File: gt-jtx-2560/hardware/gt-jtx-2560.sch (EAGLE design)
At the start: 21 parts

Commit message: added new files
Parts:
- removed LCD1: LCD-G12864-BARE, SparkFun-Displays:LCD-G12864-BARE
- added J1: (no value), SparkFun-Connectors:CONN_20
- added R1: 2.2K, resistor:R-US_0204/5
- added R2: 1K, resistor:R-US_0204/5
- added ROT_1, ROT_2: rgSbVBCA, Rembrandt Electronics - JST XH Connectors v1-0:JST-XH-08-PIN-LONG-PAD
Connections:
- new net N$31: B1.15(RX3), ROT_1-3.S
- new net N$47: B1.14(TX3), ROT_2-3.S
- new net N$48: B1.2, ROT_1-8.S
- new net N$49: B1.3, ROT_1-6.S
- new net N$50: B1.19(RX1), ROT_2-8.S
- new net N$51: B1.18(TX1), ROT_2-6.S
- new net N$52: J1.19, R1.1
- new net N$53: B1.30, J1.6
- new net N$54: B1.31, J1.16
- new net N$55: B1.32, J1.4
- new net N$56: B1.33, J1.17
- new net N$57: B1.34, J1.15
- new net N$58: J1.5, R2.1
- net N$1: now also J1.7; no longer LCD1.DB0
- net N$2: now also J1.8; no longer LCD1.DB1
- net N$3: now also J1.9; no longer LCD1.DB2
- net N$4: now also J1.10; no longer LCD1.DB3
- net N$43: now also J1.1, J1.20, R2.2, ROT_1-7.S, ROT_2-7.S
- net N$44: now also J1.2, R1.2, ROT_1-5.S, ROT_2-5.S
- net N$5: now also J1.11; no longer LCD1.DB4
- net N$6: now also J1.12; no longer LCD1.DB5
- net N$7: now also J1.13; no longer LCD1.DB6
- net N$8: now also J1.14; no longer LCD1.DB7
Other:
- moved on the sheet: NAVI-7

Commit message: added case design, changed the schematic for lcd
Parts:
- added ID1, ID2: JST-XH-03-PIN-LONG-PAD, Rembrandt Electronics - JST XH Connectors v1-0:JST-XH-03-PIN-LONG-PAD
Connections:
- removed net N$43: AIL-3.S, AIL_DR-3.S, B1.GND@0, B1.GND@1, B1.GND@2, B1.GND@3, B1.GND@4, ELE-3.S, ELE_DR-3.S, GEAR-3.S, H_B-3.S, J1.1, J1.20, NAVI-8.S, POT1-3.S, POT2-3.S, POT3-3.S, PPM-3.S, R2.2, ROT_1-7.S, ROT_2-7.S, RUD-3.S, RUD_DR-3.S, SD-6.S, THR-3.S, THR_X-3.S, TRIML-8.S, TRIMR-8.S, TRN-3.S
- removed net N$44: AIL-1.S, AIL_DR-1.S, B1.5V@0, B1.AREF, ELE-1.S, ELE_DR-1.S, GEAR-1.S, J1.2, NAVI-1.S, POT1-1.S, POT2-1.S, POT3-1.S, PPM-2.S, R1.2, ROT_1-5.S, ROT_2-5.S, RUD-1.S, RUD_DR-1.S, SD-5.S, THR-1.S, THR_X-1.S, TRIML-1.S, TRIMR-1.S, TRN-1.S
- new net GND: AIL-3.S, AIL_DR-3.S, B1.GND@0, B1.GND@1, B1.GND@2, B1.GND@3, B1.GND@4, ELE-3.S, ELE_DR-3.S, GEAR-3.S, H_B-3.S, ID1-3.S, ID2-3.S, J1.1, J1.20, NAVI-8.S, POT1-3.S, POT2-3.S, POT3-3.S, PPM-3.S, R2.2, ROT_1-7.S, ROT_2-7.S, RUD-3.S, RUD_DR-3.S, SD-6.S, THR-3.S, THR_X-3.S, TRIML-8.S, TRIMR-8.S, TRN-3.S
- new net N$59: B1.36, ID2-2.S
- new net N$60: B1.37, ID1-2.S
- new net VCC: AIL-1.S, AIL_DR-1.S, B1.5V@0, B1.AREF, ELE-1.S, ELE_DR-1.S, GEAR-1.S, ID1-1.S, ID2-1.S, J1.2, NAVI-1.S, POT1-1.S, POT2-1.S, POT3-1.S, PPM-2.S, R1.2, ROT_1-5.S, ROT_2-5.S, RUD-1.S, RUD_DR-1.S, SD-5.S, THR-1.S, THR_X-1.S, TRIML-1.S, TRIMR-1.S, TRN-1.S
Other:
- moved on the sheet: PPM-2, R1, ROT_1-1, ROT_1-2, ROT_1-4
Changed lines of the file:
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@@
 <?xml version="1.0" encoding="utf-8"?>
 <!DOCTYPE eagle SYSTEM "eagle.dtd">
-<eagle version="8.1.0">
+<eagle version="8.2.2">
 <drawing>
 <settings>
@@
 <part name="R1" library="resistor" deviceset="R-US_" device="0204/5" value="2.2K"/>
 <part name="R2" library="resistor" deviceset="R-US_" device="0204/5" value="1K"/>
+<part name="ID2" library="Rembrandt Electronics - JST XH Connectors v1-0" deviceset="JST-XH-03-PIN" device="-LONG-PAD" value=""/>
+<part name="ID1" library="Rembrandt Electronics - JST XH Connectors v1-0" deviceset="JST-XH-03-PIN" device="-LONG-PAD" value=""/>
 </parts>
 <sheets>
@@
 <instance part="H_B" gate="-3" x="116.84" y="15.24" rot="R90"/>
 <instance part="PPM" gate="-1" x="2.54" y="63.5" rot="R180"/>
-<instance part="PPM" gate="-2" x="132.08" y="160.02" rot="R270"/>
+<instance part="PPM" gate="-2" x="124.46" y="160.02" rot="R270"/>
 <instance part="PPM" gate="-3" x="119.38" y="15.24" rot="R90"/>
 <instance part="B1" gate="G$1" x="22.86" y="101.6"/>
@@
 <instance part="SD" gate="-7" x="-17.78" y="111.76" rot="R180"/>
 <instance part="SD" gate="-8" x="-17.78" y="109.22" rot="R180"/>
-<instance part="ROT_1" gate="-1" x="119.38" y="121.92"/>
-<instance part="ROT_1" gate="-2" x="119.38" y="119.38"/>
+<instance part="ROT_1" gate="-1" x="111.76" y="121.92"/>
+<instance part="ROT_1" gate="-2" x="111.76" y="119.38"/>
 <instance part="ROT_1" gate="-3" x="43.18" y="147.32"/>
-<instance part="ROT_1" gate="-4" x="119.38" y="114.3"/>
+<instance part="ROT_1" gate="-4" x="111.76" y="114.3"/>
 <instance part="ROT_1" gate="-5" x="93.98" y="160.02" rot="R270"/>
 <instance part="ROT_1" gate="-6" x="2.54" y="86.36" rot="R180"/>
@@
 <attribute name="NAME" x="81.28" y="93.472" size="1.778" layer="95" font="vector" rot="R180"/>
 </instance>
-<instance part="R1" gate="G$1" x="129.54" y="99.06"/>
+<instance part="R1" gate="G$1" x="116.84" y="99.06"/>
 <instance part="R2" gate="G$1" x="86.36" y="139.7" rot="R90"/>
+<instance part="ID2" gate="-1" x="139.7" y="160.02" rot="MR270"/>
+<instance part="ID2" gate="-2" x="43.18" y="93.98" rot="MR180"/>
+<instance part="ID2" gate="-3" x="139.7" y="15.24" rot="MR90"/>
+<instance part="ID1" gate="-1" x="137.16" y="160.02" rot="MR270"/>
+<instance part="ID1" gate="-2" x="43.18" y="91.44" rot="MR180"/>
+<instance part="ID1" gate="-3" x="142.24" y="15.24" rot="MR90"/>
 </instances>
 <busses>
@@
 </segment>
 </net>
-<net name="N$43" class="0">
+<net name="GND" class="0">
 <segment>
 <pinref part="B1" gate="G$1" pin="GND@0"/>
@@
 <junction x="116.84" y="12.7"/>
 <pinref part="PPM" gate="-3" pin="S"/>
-<wire x1="119.38" y1="12.7" x2="147.32" y2="12.7" width="0.1524" layer="91"/>
+<wire x1="119.38" y1="12.7" x2="139.7" y2="12.7" width="0.1524" layer="91"/>
 <junction x="119.38" y="12.7"/>
+<wire x1="139.7" y1="12.7" x2="142.24" y2="12.7" width="0.1524" layer="91"/>
+<wire x1="142.24" y1="12.7" x2="147.32" y2="12.7" width="0.1524" layer="91"/>
 <wire x1="5.08" y1="50.8" x2="5.08" y2="12.7" width="0.1524" layer="91"/>
 <junction x="5.08" y="50.8"/>
@@
 <pinref part="R2" gate="G$1" pin="2"/>
 <junction x="86.36" y="144.78"/>
-</segment>
-</net>
-<net name="N$44" class="0">
+<pinref part="ID1" gate="-3" pin="S"/>
+<junction x="142.24" y="12.7"/>
+<pinref part="ID2" gate="-3" pin="S"/>
+<junction x="139.7" y="12.7"/>
+</segment>
+</net>
+<net name="VCC" class="0">
 <segment>
 <wire x1="0" y1="139.7" x2="0" y2="149.86" width="0.1524" layer="91"/>
@@
 <junction x="144.78" y="162.56"/>
 <pinref part="POT3" gate="-1" pin="S"/>
-<wire x1="142.24" y1="162.56" x2="137.16" y2="162.56" width="0.1524" layer="91"/>
+<wire x1="142.24" y1="162.56" x2="139.7" y2="162.56" width="0.1524" layer="91"/>
 <junction x="142.24" y="162.56"/>
 <pinref part="GEAR" gate="-1" pin="S"/>
-<wire x1="137.16" y1="162.56" x2="132.08" y2="162.56" width="0.1524" layer="91"/>
+<wire x1="139.7" y1="162.56" x2="137.16" y2="162.56" width="0.1524" layer="91"/>
+<wire x1="137.16" y1="162.56" x2="129.54" y2="162.56" width="0.1524" layer="91"/>
+<wire x1="129.54" y1="162.56" x2="124.46" y2="162.56" width="0.1524" layer="91"/>
 <wire x1="157.48" y1="162.56" x2="160.02" y2="162.56" width="0.1524" layer="91"/>
 <junction x="157.48" y="162.56"/>
@@
 <junction x="160.02" y="162.56"/>
 <pinref part="PPM" gate="-2" pin="S"/>
-<wire x1="114.3" y1="162.56" x2="132.08" y2="162.56" width="0.1524" layer="91"/>
+<wire x1="114.3" y1="162.56" x2="124.46" y2="162.56" width="0.1524" layer="91"/>
 <junction x="114.3" y="162.56"/>
-<junction x="132.08" y="162.56"/>
+<junction x="124.46" y="162.56"/>
 <pinref part="TRIMR" gate="-1" pin="S"/>
 <junction x="109.22" y="162.56"/>
@@
 <wire x1="66.04" y1="142.24" x2="66.04" y2="162.56" width="0.1524" layer="91"/>
 <junction x="66.04" y="162.56"/>
-<wire x1="134.62" y1="99.06" x2="137.16" y2="99.06" width="0.1524" layer="91"/>
-<wire x1="137.16" y1="99.06" x2="137.16" y2="162.56" width="0.1524" layer="91"/>
+<wire x1="121.92" y1="99.06" x2="129.54" y2="99.06" width="0.1524" layer="91"/>
+<wire x1="129.54" y1="99.06" x2="129.54" y2="162.56" width="0.1524" layer="91"/>
+<junction x="129.54" y="162.56"/>
+<pinref part="R1" gate="G$1" pin="2"/>
+<pinref part="ID2" gate="-1" pin="S"/>
+<junction x="139.7" y="162.56"/>
+<pinref part="ID1" gate="-1" pin="S"/>
 <junction x="137.16" y="162.56"/>
-<pinref part="R1" gate="G$1" pin="2"/>
 </segment>
 </net>
@@
 <segment>
 <pinref part="J1" gate="G$1" pin="19"/>
-<wire x1="71.12" y1="99.06" x2="124.46" y2="99.06" width="0.1524" layer="91"/>
+<wire x1="71.12" y1="99.06" x2="111.76" y2="99.06" width="0.1524" layer="91"/>
 <pinref part="R1" gate="G$1" pin="1"/>
 </segment>
@@
 </segment>
 </net>
+<net name="N$59" class="0">
+<segment>
+<pinref part="B1" gate="G$1" pin="36"/>
+<pinref part="ID2" gate="-2" pin="S"/>
+</segment>
+</net>
+<net name="N$60" class="0">
+<segment>
+<pinref part="B1" gate="G$1" pin="37"/>
+<pinref part="ID1" gate="-2" pin="S"/>
+</segment>
+</net>

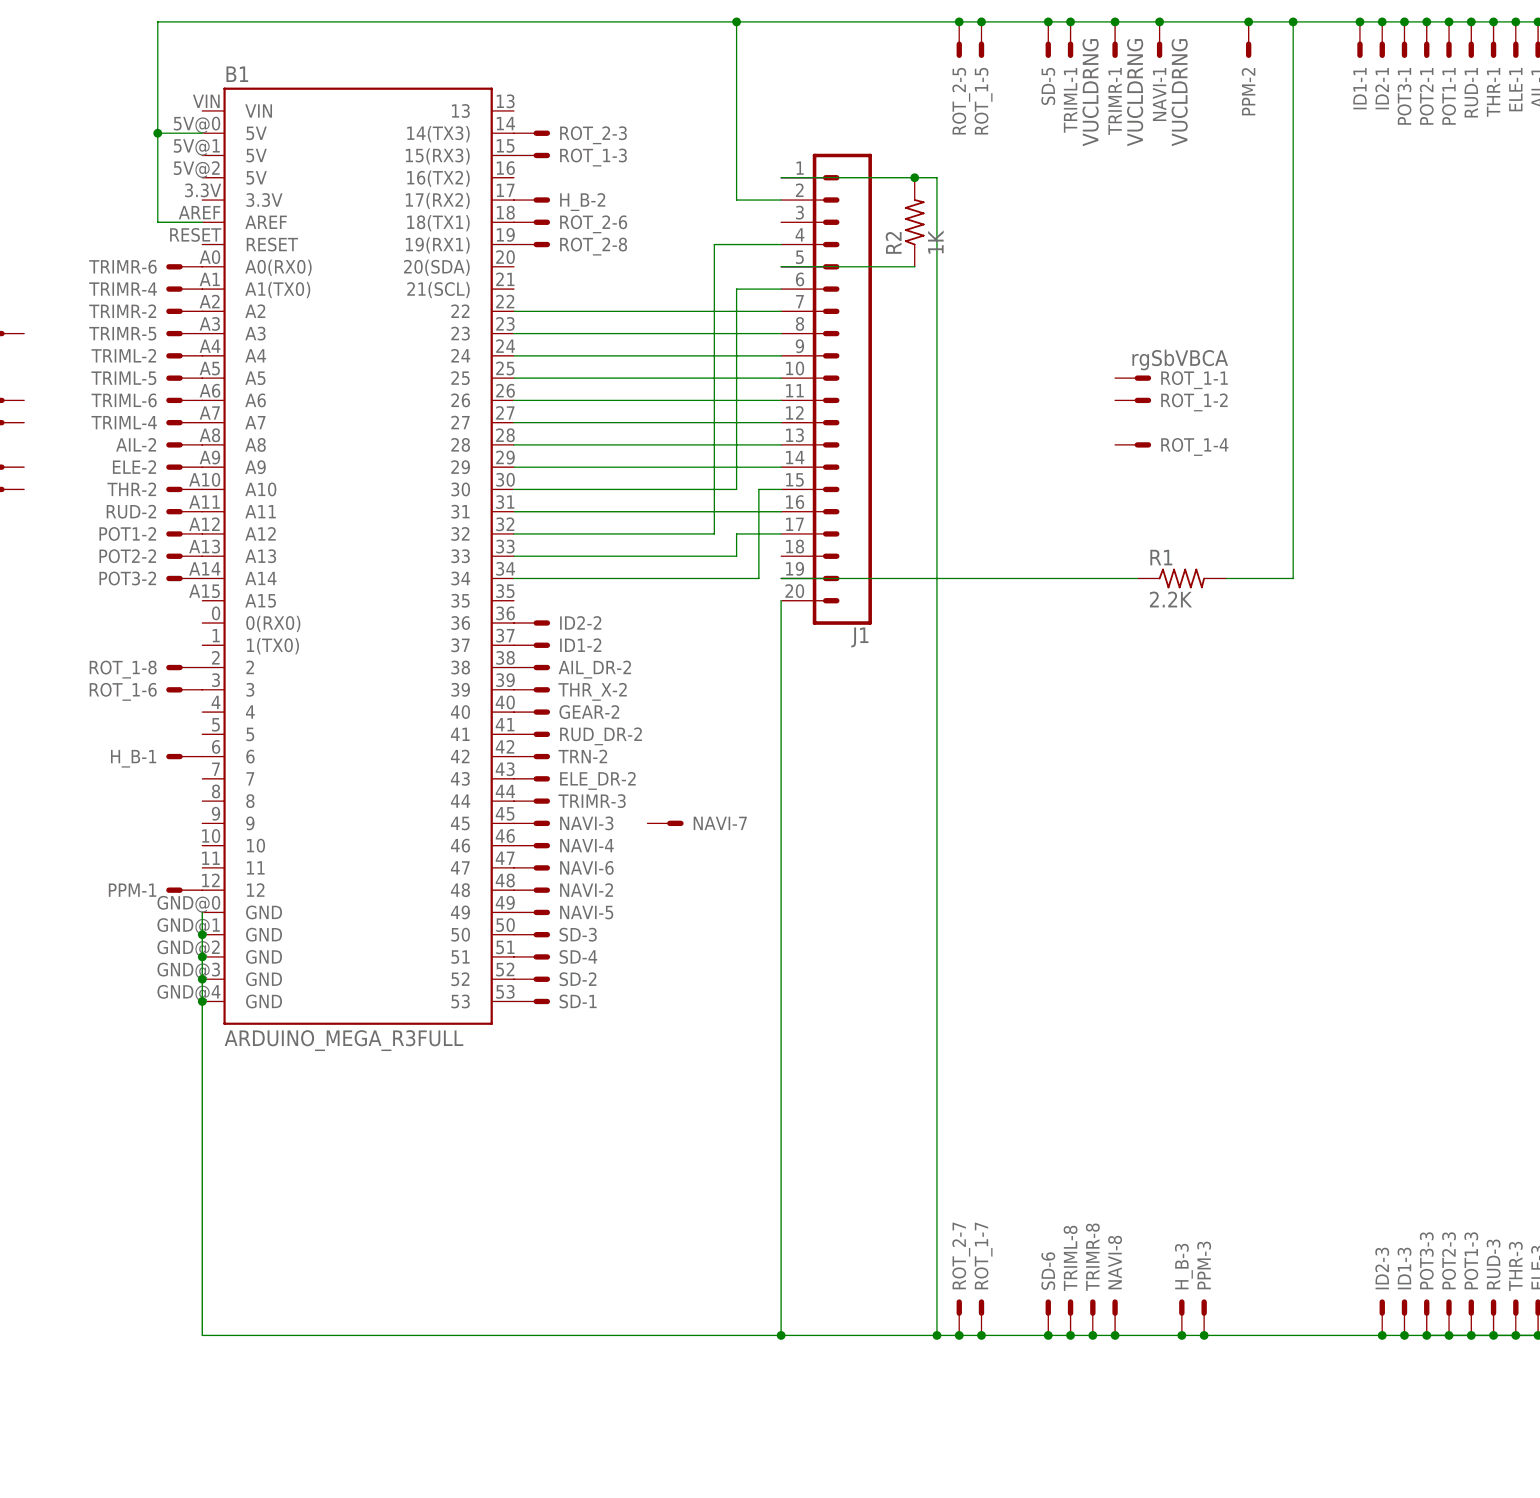
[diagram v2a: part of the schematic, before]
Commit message: fixed LCD connections and added connector for contrast adjustment
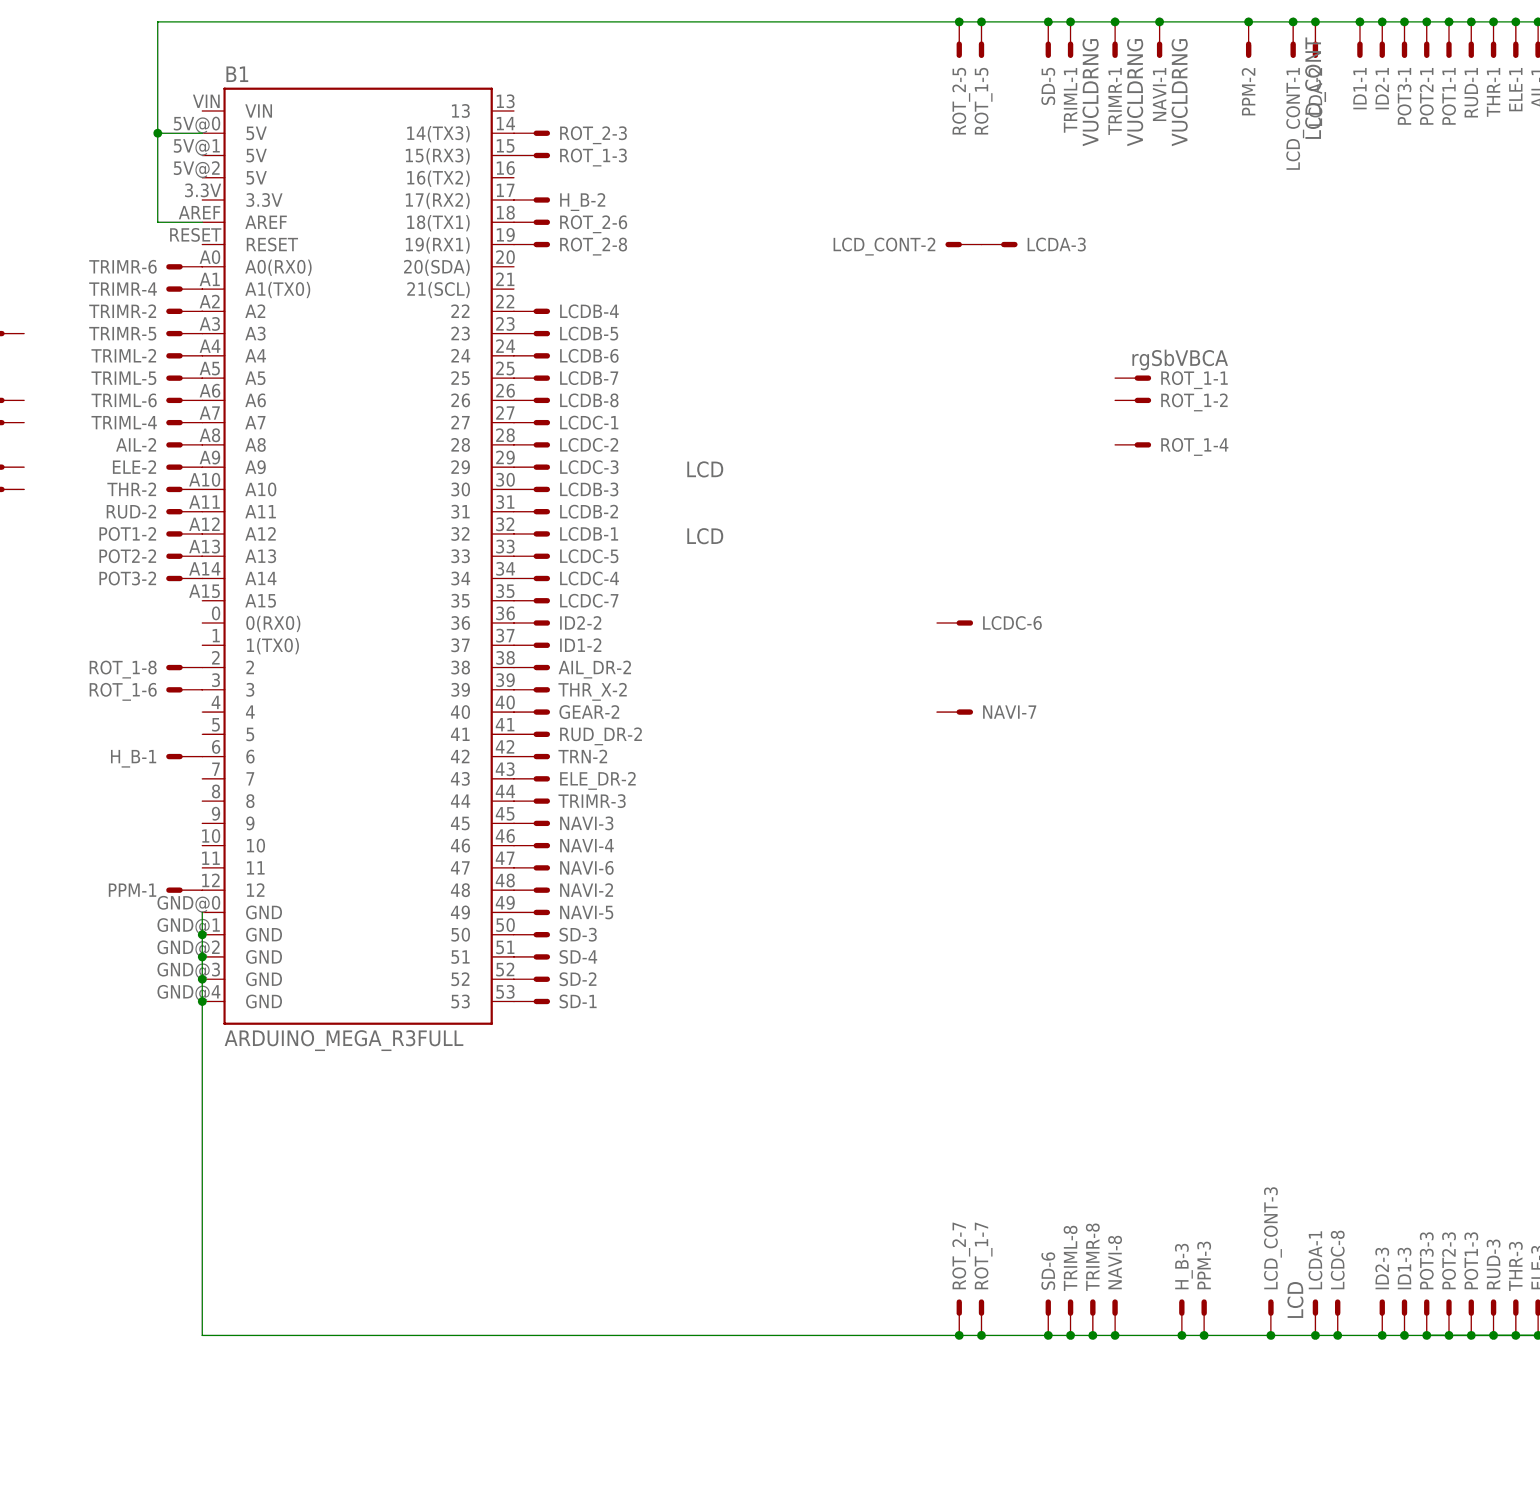
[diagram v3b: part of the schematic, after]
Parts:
- removed J1: (no value), SparkFun-Connectors:CONN_20
- removed R1: 2.2K, resistor:R-US_0204/5
- removed R2: 1K, resistor:R-US_0204/5
- added LCDA: LCD, Rembrandt Electronics - JST XH Connectors v1-0:JST-XH-03-PIN-LONG-PAD
- added LCDB, LCDC: LCD, Rembrandt Electronics - JST XH Connectors v1-0:JST-XH-08-PIN-LONG-PAD
- added LCD_CONT: LCD_CONT, Rembrandt Electronics - JST XH Connectors v1-0:JST-XH-03-PIN-LONG-PAD
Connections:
- removed net N$57: B1.34, J1.15
- removed net N$58: J1.5, R2.1
- new net N$43: B1.30, LCDB-3.S
- new net N$44: B1.31, LCDB-2.S
- net GND: now also LCDA-1.S, LCDC-8.S, LCD_CONT-3.S; no longer J1.1, J1.20, R2.2
- net N$1: now also LCDB-4.S; no longer J1.7
- net N$2: now also LCDB-5.S; no longer J1.8
- net N$3: now also LCDB-6.S; no longer J1.9
- net N$4: now also LCDB-7.S; no longer J1.10
- net N$5: now also LCDB-8.S; no longer J1.11
- net N$52: now also B1.32, LCDB-1.S; no longer J1.19, R1.1
- net N$53: now also B1.34, LCDC-4.S; no longer B1.30, J1.6
- net N$54: now also B1.33, LCDC-5.S; no longer B1.31, J1.16
- net N$55: now also B1.35, LCDC-7.S; no longer B1.32, J1.4
- net N$56: now also LCDA-3.S, LCD_CONT-2.S; no longer B1.33, J1.17
- net N$6: now also LCDC-1.S; no longer J1.12
- net N$7: now also LCDC-2.S; no longer J1.13
- net N$8: now also LCDC-3.S; no longer J1.14
- net VCC: now also LCDA-2.S, LCD_CONT-1.S; no longer J1.2, R1.2
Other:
- moved on the sheet: NAVI-7

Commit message: added sim connector
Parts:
- added X1: SIM, adafruit:STEREOJACK
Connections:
- new net N$57: PPM-1.S, X1.3
- net GND: now also X1.1
- net N$39: now also X1.2; no longer PPM-1.S
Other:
- moved on the sheet: PPM-1
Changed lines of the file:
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@@
 <layer number="230" name="230bmp" color="7" fill="1" visible="yes" active="yes"/>
 <layer number="231" name="231bmp" color="7" fill="1" visible="yes" active="yes"/>
+<layer number="232" name="Eagle3D_PG2" color="7" fill="1" visible="no" active="no"/>
+<layer number="233" name="Eagle3D_PG3" color="7" fill="1" visible="no" active="no"/>
 <layer number="248" name="Housing" color="7" fill="1" visible="yes" active="yes"/>
 <layer number="249" name="Edge" color="7" fill="1" visible="yes" active="yes"/>
@@
 <part name="LCDA" library="Rembrandt Electronics - JST XH Connectors v1-0" deviceset="JST-XH-03-PIN" device="-LONG-PAD" value="LCD"/>
 <part name="LCD_CONT" library="Rembrandt Electronics - JST XH Connectors v1-0" deviceset="JST-XH-03-PIN" device="-LONG-PAD" value="LCD_CONT"/>
+<part name="X1" library="adafruit" deviceset="STEREOJACK" device="" value="SIM"/>
 </parts>
 <sheets>
@@
 <instance part="H_B" gate="-2" x="43.18" y="142.24"/>
 <instance part="H_B" gate="-3" x="116.84" y="15.24" rot="R90"/>
-<instance part="PPM" gate="-1" x="2.54" y="63.5" rot="R180"/>
+<instance part="PPM" gate="-1" x="-10.16" y="60.96"/>
 <instance part="PPM" gate="-2" x="124.46" y="160.02" rot="R270"/>
 <instance part="PPM" gate="-3" x="119.38" y="15.24" rot="R90"/>
@@
 <instance part="LCD_CONT" gate="-2" x="91.44" y="137.16" rot="R180"/>
 <instance part="LCD_CONT" gate="-3" x="127" y="15.24" rot="R90"/>
+<instance part="X1" gate="1" x="-30.48" y="58.42" rot="R180"/>
 </instances>
 <busses>
@@
 <pinref part="B1" gate="G$1" pin="A0(RX0)"/>
 <pinref part="TRIMR" gate="-6" pin="S"/>
-</segment>
-</net>
-<net name="N$39" class="0">
-<segment>
-<pinref part="B1" gate="G$1" pin="12"/>
-<pinref part="PPM" gate="-1" pin="S"/>
 </segment>
 </net>
@@
 <pinref part="LCD_CONT" gate="-3" pin="S"/>
 <junction x="127" y="12.7"/>
+<pinref part="X1" gate="1" pin="1"/>
+<wire x1="-17.78" y1="66.04" x2="-15.24" y2="66.04" width="0.1524" layer="91"/>
+<wire x1="-15.24" y1="66.04" x2="-15.24" y2="12.7" width="0.1524" layer="91"/>
+<wire x1="-15.24" y1="12.7" x2="5.08" y2="12.7" width="0.1524" layer="91"/>
+<junction x="5.08" y="12.7"/>
 </segment>
 </net>
@@
 </segment>
 </net>
+<net name="N$57" class="0">
+<segment>
+<pinref part="X1" gate="1" pin="3"/>
+<pinref part="PPM" gate="-1" pin="S"/>
+<wire x1="-12.7" y1="60.96" x2="-17.78" y2="60.96" width="0.1524" layer="91"/>
+</segment>
+</net>
+<net name="N$39" class="0">
+<segment>
+<pinref part="X1" gate="1" pin="2"/>
+<pinref part="B1" gate="G$1" pin="12"/>
+<wire x1="-17.78" y1="63.5" x2="5.08" y2="63.5" width="0.1524" layer="91"/>
+</segment>
+</net>
